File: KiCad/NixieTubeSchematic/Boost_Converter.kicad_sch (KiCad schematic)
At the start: 32 parts

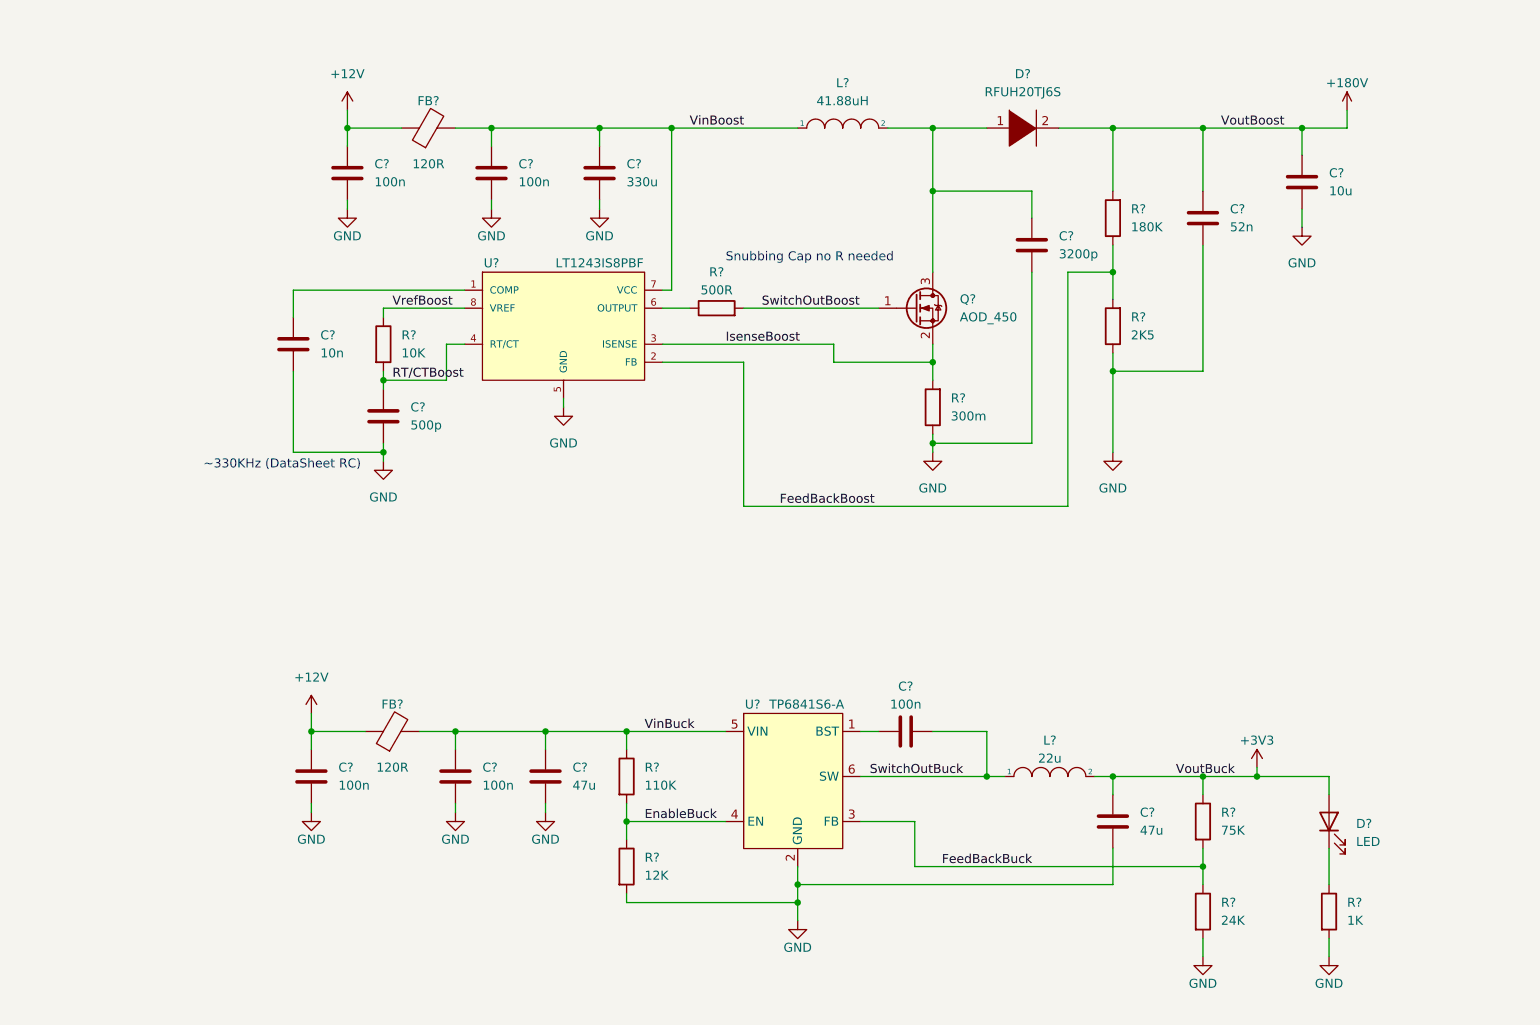
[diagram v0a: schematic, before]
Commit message: Schematic for DS3231 RTC and AT24C32 EEPROM added
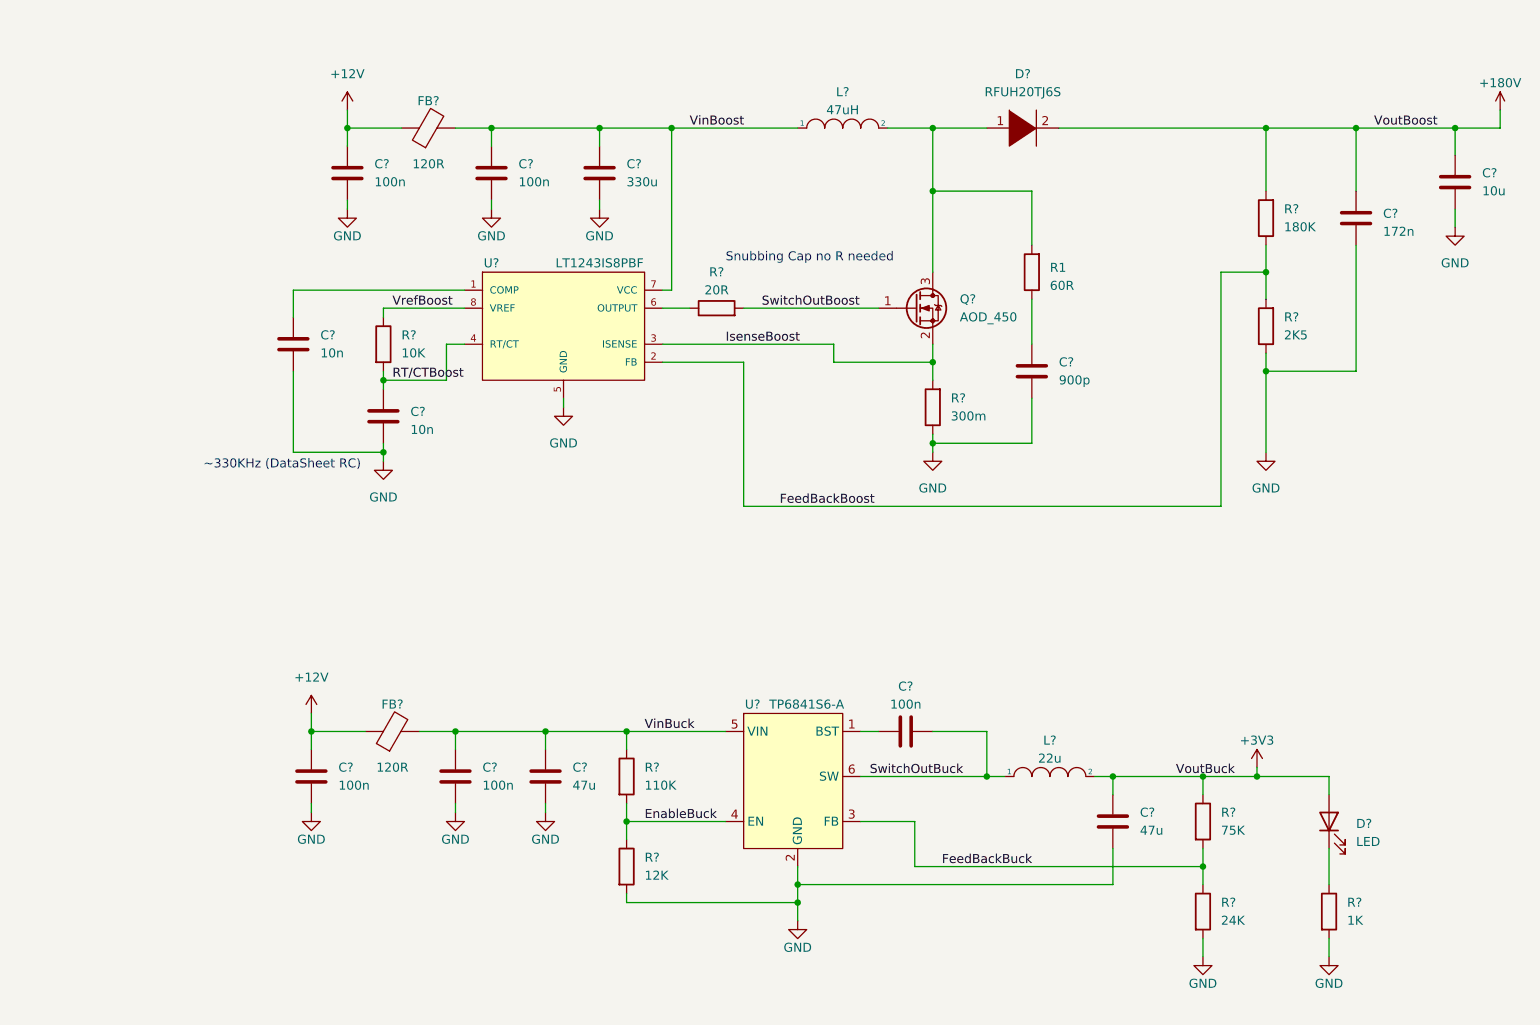
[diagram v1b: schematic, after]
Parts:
- added R1: 60R, symbol Device:R
- C?: value 52n -> 172n
- C?: value 500p -> 10n
- C?: value 3200p -> 900p
- L?: value 41.88uH -> 47uH
- R?: value 500R -> 20R
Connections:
- net at D?.1 (K), L?.2, Q?.3 (D): now also R1.2; no longer C?.1
- new net: C?.1, R1.1
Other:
- moved on the sheet: C?, R?

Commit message: Small changes
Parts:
- added D2: 1N914, Diode_THT:D_DO-35_SOD27_P7.62mm_Horizontal, symbol Diode:1N914
- added Q5: PNP, symbol Simulation_SPICE:PNP
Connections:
- net GND: now also Q5.3 (E)
- net SwitchOutBoost: now also D2.2 (A), Q5.2 (B); no longer Q?.1 (G)
- new net: D2.1 (K), Q5.1 (C), Q?.1 (G)
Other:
- note added: "Isense: (current sense TH) / ILmax 1V / 1.94A 0.515R 0.515R/2 = 257m Rsense use 300"
- note added: "NIXIELOAD: Internal Nixie pin impedance ~37K 26K load resistor for each pin for ~2.8A draw 6 Nixte tubes in parallel expected load 4K3"
- note added: "Snubbing circuit"
- note removed: "Snubbing Cap no R needed"
- moved on the sheet: C?, D?, FB?, L?, Q?, R1, R?, U?
